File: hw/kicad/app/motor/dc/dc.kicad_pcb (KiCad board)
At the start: 2 copper layers, 50 x 50 mm, 22 parts, among them J1 TOP, J2 Motor 1, J3 Motor 2, J4 Motor 3, J5 Motor 4, J6 BOTTUM, U1 DRV8870DDA, U2 DRV8870DDA, U3 DRV8870DDA, U4 DRV8870DDA

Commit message: 修改尺寸至45x45
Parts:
- C10, C11, C12, C2, C4, C6, C8, C9: footprint Capacitor_SMD:C_0603_1608Metric -> Capacitor_SMD:C_0805_2012Metric
- moved C8 11.0 mm to (83.8, 60.6)
- moved C6 10.9 mm to (83.7, 48.5)
- moved C2 9.27 mm to (66.1, 48.5)
- moved C4 8.89 mm to (66.2, 60.5)
- moved C12 3.57 mm to (80.8, 67.9), turned to 180 degrees
- moved C10 3.10 mm to (63.0, 67.9), turned to 180 degrees
- moved J2 2.87 mm to (60.7, 41.3)
- moved J5 2.83 mm to (90.8, 41.3)
- moved J3 2.81 mm to (70.8, 41.3)
- moved J4 2.80 mm to (80.8, 41.3)
- moved C11 2.78 mm to (82.0, 55.8), turned to 180 degrees
- moved C1 2.39 mm to (71.0, 51.0)
- moved U3 2.33 mm to (79.6, 50.4)
- moved C3 2.05 mm to (71.1, 63.0)
- moved J1 2.00 mm to (75.7, 75.2)
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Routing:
- net /PWM_4: track 16.4 -> 22.3 mm
- net /PWM_3: track 21.3 -> 25.5 mm
- net GND: track 3.84 -> 0.00 mm, vias 53 -> 40
- net +3.3V: track 74.6 -> 71.4 mm, vias 7 -> 10
- net /PWM_6: track 24.5 -> 22.3 mm
- net /OUT3: track 26.4 -> 28.4 mm
- net /PWM_5: track 27.7 -> 26.0 mm
- net /PWM_8: track 11.7 -> 9.98 mm
- net /OUT2: track 6.44 -> 4.79 mm
- net /PWM_7: track 15.0 -> 13.3 mm
- net /OUT1: track 5.90 -> 4.27 mm
- net /PWM_2: track 36.1 -> 34.7 mm
- net /OUT6: track 5.89 -> 4.81 mm
- net /PWM_1: track 39.1 -> 38.1 mm
- net /OUT4: track 24.8 -> 25.4 mm
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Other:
- board size 50 x 50 mm -> 45 x 47.5 mm

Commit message: Pindar v1.0
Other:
- board text added: "Pindar v1.0 Type APP Mecanum wheel v1.0"
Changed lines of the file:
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@@
   (gr_circle locked (center 75.72 75.22) (end 76.72 75.22)
     (stroke (width 0.15) (type default)) (fill none) (layer "User.1"))
+  (gr_text "Pindar v1.0 \nType APP\nMecanum wheel v1.0" (at 70.9956 42.2148) (layer "B.SilkS")
+    (effects (font (size 1 1) (thickness 0.15)) (justify left bottom mirror))
+  )
   (segment (start 80.165 75.2348) (end 80.165 77.17) (width 0.762) (layer "F.Cu") (net 1))
   (segment (start 81.5112 67.6554) (end 81.75 67.8942) (width 0.381) (layer "F.Cu") (net 1))

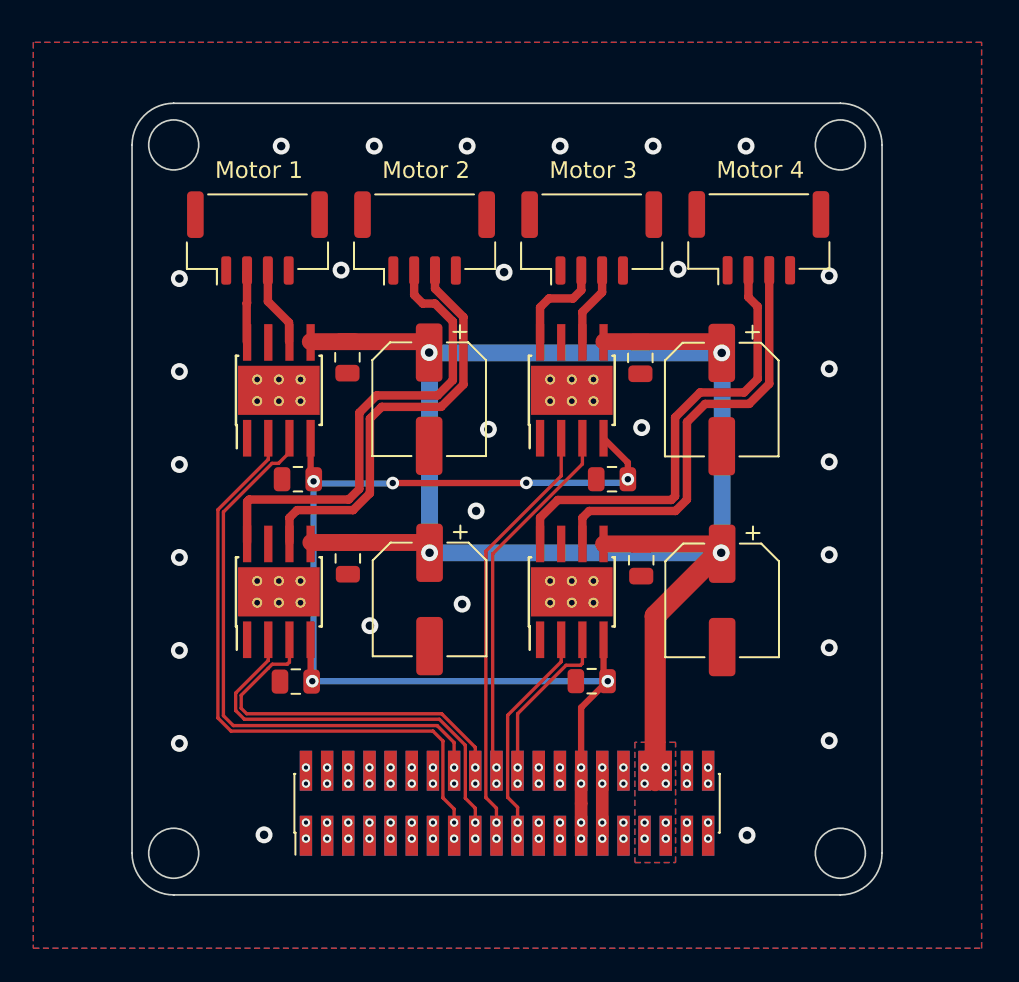
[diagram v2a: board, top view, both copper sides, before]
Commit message: 第二次打样的整改；dc motor改成了三路 io不够做不了四路；
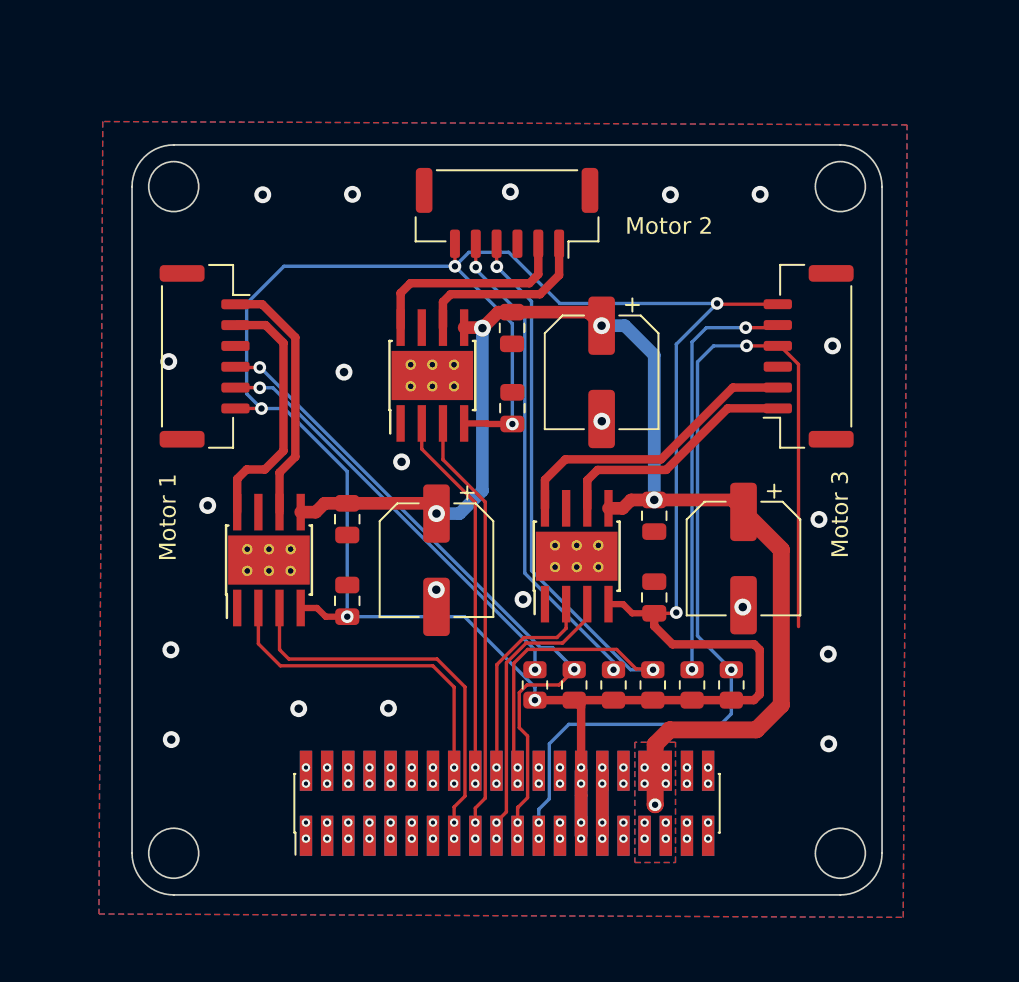
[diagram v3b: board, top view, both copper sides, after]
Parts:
- removed C12, C8: 0.1uF, Capacitor_SMD:C_0805_2012Metric
- removed C7: 10uF, Capacitor_SMD:CP_Elec_6.3x5.4
- removed J5: Motor 4, Connector_JST:JST_GH_BM04B-GHS-TBT_1x04-1MP_P1.25mm_Vertical
- removed U4: DRV8870DDA, Package_SO:Texas_HTSOP-8-1EP_3.9x4.9mm_P1.27mm_EP2.95x4.9mm_Mask2.4x3.1mm_ThermalVias
- added R1: R, Resistor_SMD:R_0805_2012Metric, F.Cu at (79.8, 68.1)
- added R2: R, Resistor_SMD:R_0805_2012Metric, F.Cu at (77.4, 68.1)
- added R3: R, Resistor_SMD:R_0805_2012Metric, F.Cu at (82.1, 68.1)
- added R4: R, Resistor_SMD:R_0805_2012Metric, F.Cu at (84.5, 68.1)
- added R5: R, Resistor_SMD:R_0805_2012Metric, F.Cu at (86.8, 68.1)
- added R6: R, Resistor_SMD:R_0805_2012Metric, F.Cu at (89.2, 68.1)
- J: renamed from J2; footprint Connector_JST:JST_GH_BM04B-GHS-TBT_1x04-1MP_P1.25mm_Vertical -> Connector_JST:JST_GH_SM06B-GHS-TB_1x06-1MP_P1.25mm_Horizontal
- J3, J4: footprint Connector_JST:JST_GH_BM04B-GHS-TBT_1x04-1MP_P1.25mm_Vertical -> Connector_JST:JST_GH_SM06B-GHS-TB_1x06-1MP_P1.25mm_Horizontal
- moved C10 20.9 mm to (76.0, 51.5), turned to 90 degrees
- moved C3 17.1 mm to (81.4, 49.4)
- moved C4 17.0 mm to (76.0, 46.7)
- moved U2 15.9 mm to (71.2, 49.6)
- moved J4 14.8 mm to (93.8, 48.4), turned to 90 degrees
- moved U1 10.2 mm to (61.4, 60.6)
- moved U3 9.96 mm to (79.9, 60.4)
- moved C2 9.71 mm to (66.1, 58.2)
- moved C1 9.67 mm to (71.5, 60.6)
- moved C5 9.63 mm to (89.9, 60.5)
- moved C6 9.51 mm to (84.6, 58.0)
- moved C9 7.87 mm to (66.1, 63.1), turned to 90 degrees
- moved J 7.78 mm to (57.6, 48.4), turned to -90 degrees
- moved C11 7.53 mm to (84.6, 62.9), turned to 90 degrees
- moved J3 5.17 mm to (75.7, 39.8), turned to 180 degrees
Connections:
- J pad 1: GND -> /OUT1
- J pad 2: /OUT1 -> /OUT2
- J pad 3: /OUT2 -> GND
- J pad 4: GND -> /ENC_1B
- J pad MP: (no net) -> GND
- J1 pad 15: /PWM_1 -> /GPIO_1
- J1 pad 16: /PWM_2 -> /GPIO_2
- J1 pad 17: /PWM_3 -> /GPIO_3
- J1 pad 18: /PWM_4 -> /GPIO_4
- J1 pad 19: /PWM_5 -> /GPIO_5
- J1 pad 20: /PWM_6 -> /GPIO_6
- J1 pad 21: /PWM_7 -> /ENC_1B
- J1 pad 22: /PWM_8 -> /ENC_2B
- J3 pad 1: GND -> /OUT3
- J3 pad 2: /OUT3 -> /OUT4
- J3 pad 3: /OUT4 -> GND
- J3 pad 4: GND -> /ENC_2B
- J3 pad MP: (no net) -> GND
- J4 pad 1: GND -> /OUT5
- J4 pad 2: /OUT5 -> /OUT6
- J4 pad 3: /OUT6 -> GND
- J4 pad 4: GND -> /CAN_H
- J4 pad MP: (no net) -> GND
- J6 pad 15: /PWM_2 -> /GPIO_2
- J6 pad 16: /PWM_1 -> /GPIO_1
- J6 pad 17: /PWM_4 -> /GPIO_4
- J6 pad 18: /PWM_3 -> /GPIO_3
- J6 pad 19: /PWM_6 -> /GPIO_6
- J6 pad 20: /PWM_5 -> /GPIO_5
- J6 pad 21: /PWM_8 -> /ENC_2B
- J6 pad 22: /PWM_7 -> /ENC_1B
- U1 pad 2: /PWM_1 -> /GPIO_2
- U1 pad 3: /PWM_2 -> /GPIO_1
- U1 pad 6: /OUT2 -> /OUT1
- U1 pad 8: /OUT1 -> /OUT2
- U2 pad 2: /PWM_3 -> /GPIO_4
- U2 pad 3: /PWM_4 -> /GPIO_3
- U2 pad 6: /OUT4 -> /OUT3
- U2 pad 8: /OUT3 -> /OUT4
- U3 pad 2: /PWM_5 -> /GPIO_6
- U3 pad 3: /PWM_6 -> /GPIO_5
- U3 pad 6: /OUT6 -> /OUT5
- U3 pad 8: /OUT5 -> /OUT6
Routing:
- net +3.3V: track 71.4 -> 151.6 mm, vias 10 -> 11
- net /CAN_H: track 0.00 -> 62.1 mm, vias 2 -> 4
- net /ENC_2B: track 0.00 -> 46.0 mm, vias 0 -> 4
- net /ENC_1B: track 0.00 -> 40.8 mm, vias 0 -> 4
- net /PWM_1: track 38.1 -> 0.00 mm, vias 2 -> 0
- net /PWM_2: track 34.7 -> 0.00 mm, vias 2 -> 0
- net /ENC_2A: track 0.00 -> 29.0 mm, vias 0 -> 2
- net /OUT7: track 27.6 -> 0.00 mm
- net +BATT: track 103.3 -> 76.6 mm, vias 12 -> 13
- net /GPIO_3: track 0.00 -> 26.0 mm, vias 0 -> 2
- net /PWM_5: track 26.0 -> 0.00 mm, vias 2 -> 0
- net /ENC_1A: track 0.00 -> 25.7 mm, vias 0 -> 2
- net /OUT8: track 25.6 -> 0.00 mm
- net /PWM_3: track 25.5 -> 0.00 mm, vias 2 -> 0
- net /ENC_3A: track 0.00 -> 25.2 mm, vias 0 -> 2
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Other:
- board size 45 x 47.5 mm -> 45 x 45 mm
